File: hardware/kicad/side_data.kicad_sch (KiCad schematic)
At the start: 7 parts, among them U25 SN74LV165AD, U26 SN74LV165AD

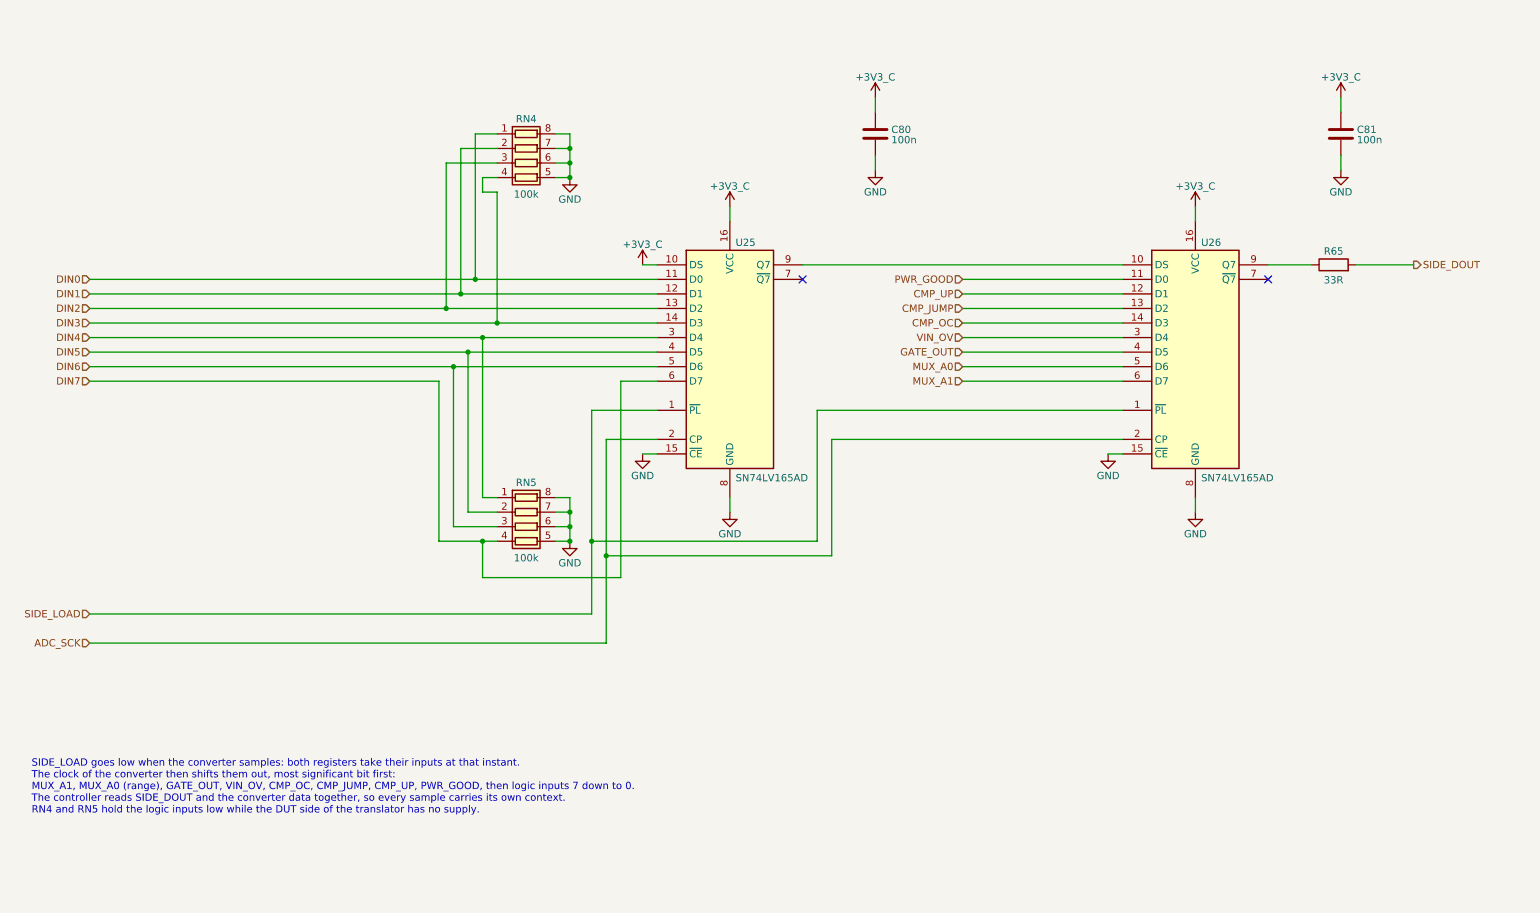
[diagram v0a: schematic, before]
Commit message: feat(hardware): draw draft A2 of the schematic
428 parts on 15 A4 pages, 14 sheets below the root sheet (D-83). Two
sheets are new: Logic Supplies, with the supervisor of the 5 V rail and
the two 3.3 V regulators, and Rail Monitor, with the comparators behind
PWR_GOOD.

The drawings follow the specification of draft A2: a current limiter
on each supply input and a priority multiplexer, a pre-regulator that
tracks the output of the linear regulator, a VIN path that withstands
-20 V to +20 V with its switch open, two diode-connected MOSFETs as
ladder clamp, thin-film and four-terminal shunts, ESD arrays at the CC
pins and at the VCC pin of the logic port. The reference designators
are numbered as KiCad numbers them (D-45), so they are not those of
draft A1.

The project library gains the symbol of the input multiplexer and two
footprints: the lever terminal block with pads of 1.9 mm x 2.3 mm and
the controller module without its antenna keep-out (D-85).

The electrical rules check reports no errors and no warnings. The
parts are candidates, and nothing is built or measured.
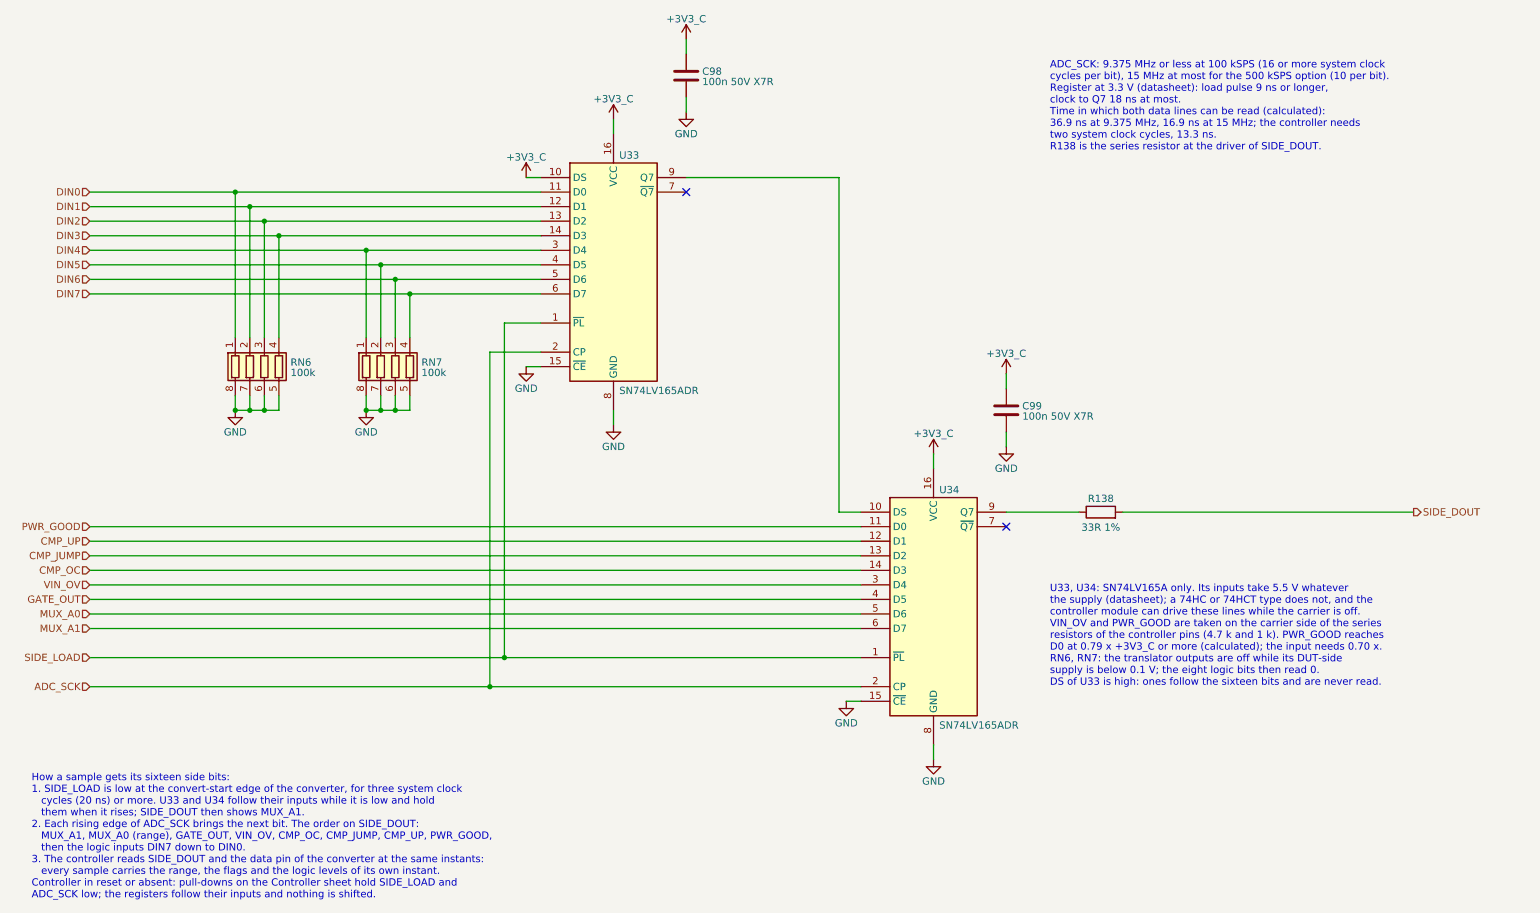
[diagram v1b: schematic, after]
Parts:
- C98: renamed from C80; value 100n -> 100n 50V X7R; MPN (none) -> C0603C104K5RACTU; Manufacturer (none) -> KEMET
- C99: renamed from C81; value 100n -> 100n 50V X7R; MPN (none) -> C0603C104K5RACTU; Manufacturer (none) -> KEMET
- R138: renamed from R65; value 33R -> 33R 1%; MPN (none) -> CRCW060333R0FKEA; Manufacturer (none) -> Vishay
- RN6: renamed from RN4; MPN (none) -> CAY16-104J4LF; Manufacturer (none) -> Bourns
- RN7: renamed from RN5; MPN (none) -> CAY16-104J4LF; Manufacturer (none) -> Bourns
- U33: renamed from U25; value SN74LV165AD -> SN74LV165ADR; Manufacturer (none) -> Texas Instruments
- U34: renamed from U26; value SN74LV165AD -> SN74LV165ADR; Manufacturer (none) -> Texas Instruments
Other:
- note added: "ADC_SCK: 9.375 MHz or less at 100 kSPS (16 or more system clock cycles per bit), 15 MHz at most for the 500 kSPS option (10 per bit). Register at 3.3 V (datasheet): load pulse 9 ns or longer, clock to Q7 18 ns at most. Time in which both data lines can be read (calculated): 36.9 ns at 9.375 MHz, 16.9 ns at 15 MHz; the controller needs two system clock cycles, 13.3 ns. R138 is the series resistor 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"
- note added: "How a sample gets its sixteen side bits: 1. SIDE_LOAD is low at the convert-start edge of the converter, for three system clock cycles (20 ns) or more. U33 and U34 follow their inputs while it is low and hold them when it rises; SIDE_DOUT then shows MUX_A1. 2. Each rising edge of ADC_SCK brings the next bit. The order on SIDE_DOUT: MUX_A1, MUX_A0 (range), GATE_OUT, VIN_OV, CMP_OC, CMP_JUMP, CMP_U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"
- note added: "U33, U34: SN74LV165A only. Its inputs take 5.5 V whatever the supply (datasheet); a 74HC or 74HCT type does not, and the controller module can drive these lines while the carrier is off. VIN_OV and PWR_GOOD are taken on the carrier side of the series resistors of the controller pins (4.7 k and 1 k). PWR_GOOD reaches D0 at 0.79 x +3V3_C or more (calculated); the input needs 0.70 x. RN6, RN7: the t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"
- note removed: "SIDE_LOAD goes low when the converter samples: both registers take their inputs at that instant. The clock of the converter then shifts them out, most significant bit first: MUX_A1, MUX_A0 (range), GATE_OUT, VIN_OV, CMP_OC, CMP_JUMP, CMP_UP, PWR_GOOD, then logic inputs 7 down to 0. The controller reads SIDE_DOUT and the converter data together, so every sample carries its own context. RN4 and RN5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"
- moved on the sheet: C98, C99, R138, RN6, RN7, U33, U34
